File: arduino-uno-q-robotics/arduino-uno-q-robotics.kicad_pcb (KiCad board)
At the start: 4 copper layers, 68.6 x 53.3 mm, 11 parts, among them J1 Conn_02x30_Odd_Even, J2 Conn_02x30_Odd_Even, J3 Connector_FFC-FPC, J4 Connector_FFC-FPC, J5 Conn_02x13_Odd_Even, J6 Conn_02x04_Odd_Even, U1 LSM6DSO32

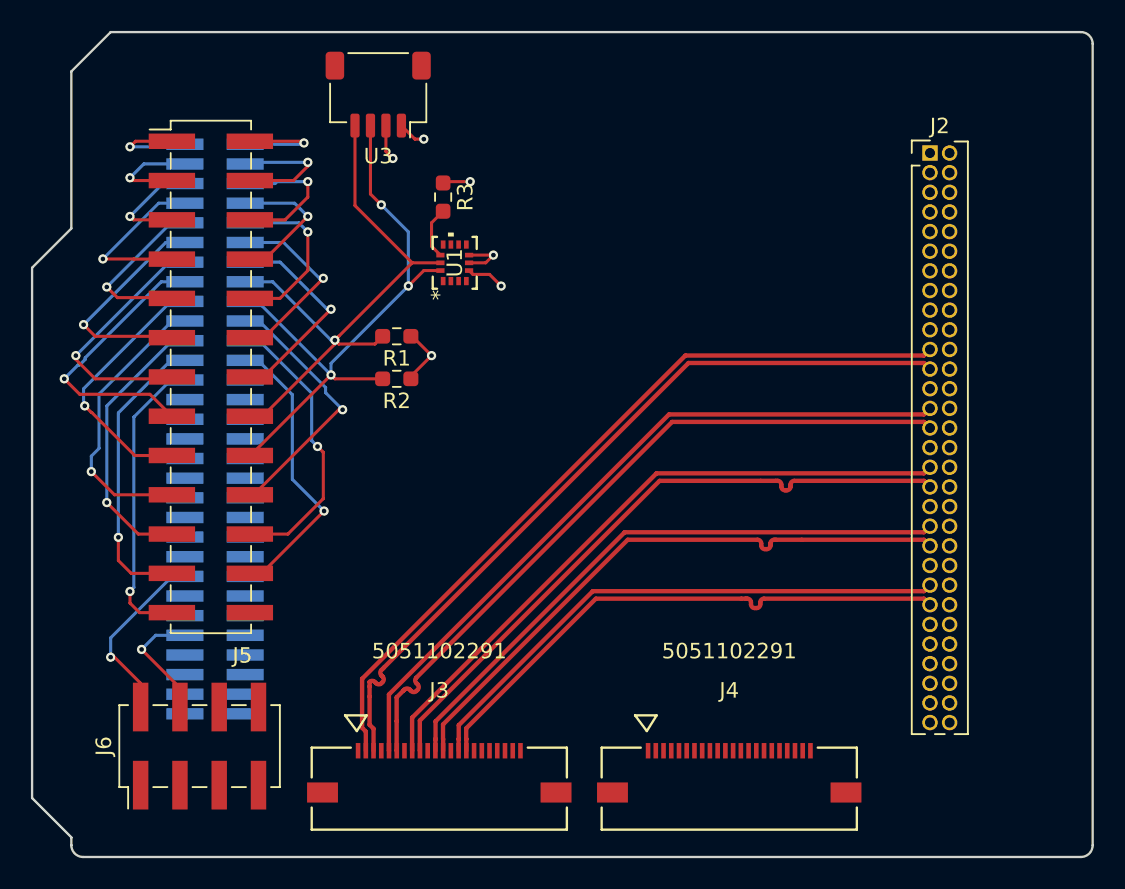
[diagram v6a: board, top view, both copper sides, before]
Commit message: Adjust JMISC/JMEDIA header spacing
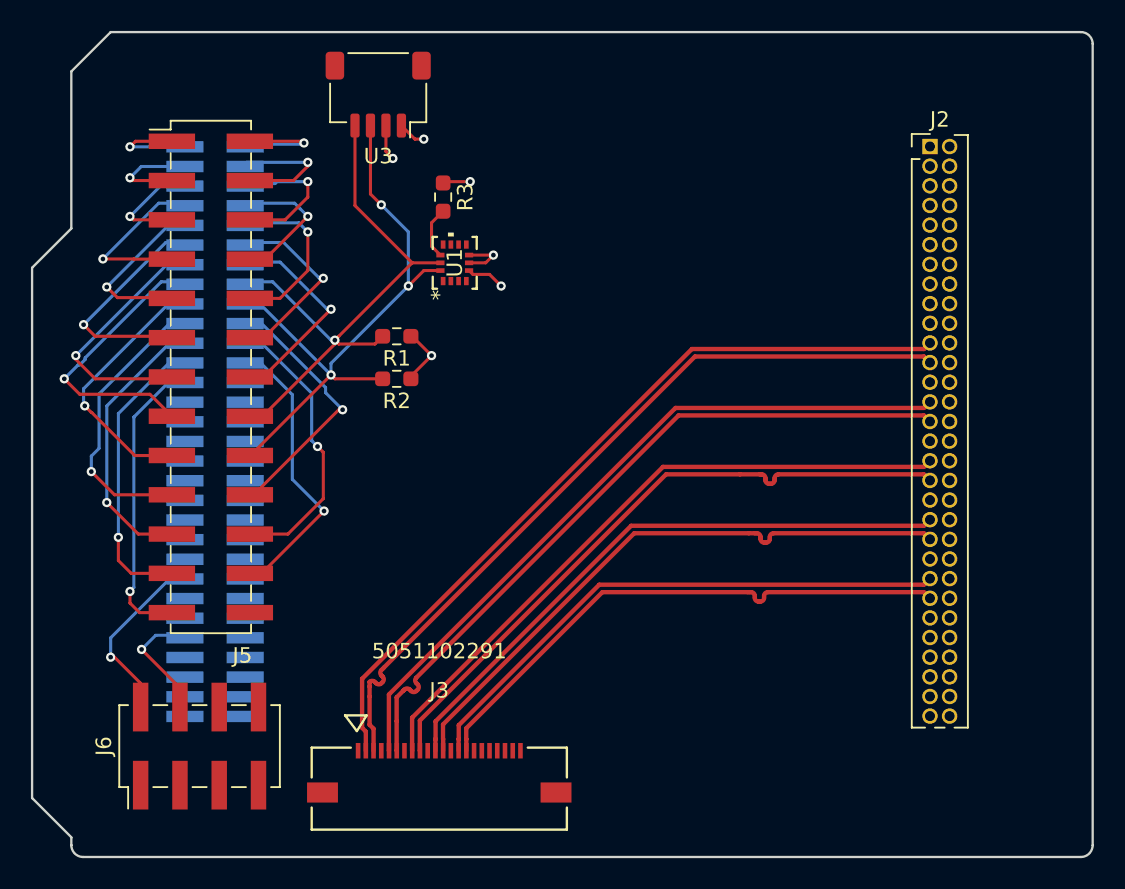
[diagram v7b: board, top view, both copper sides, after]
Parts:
- removed J4: Connector_FFC-FPC, robotics-footprints:CON_5051102291_MOL
- moved J2 0.42 mm to (172.5, 75.0)
- moved J1 0.17 mm to (126.2, 93.4)

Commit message: Add missing components to PCB editor
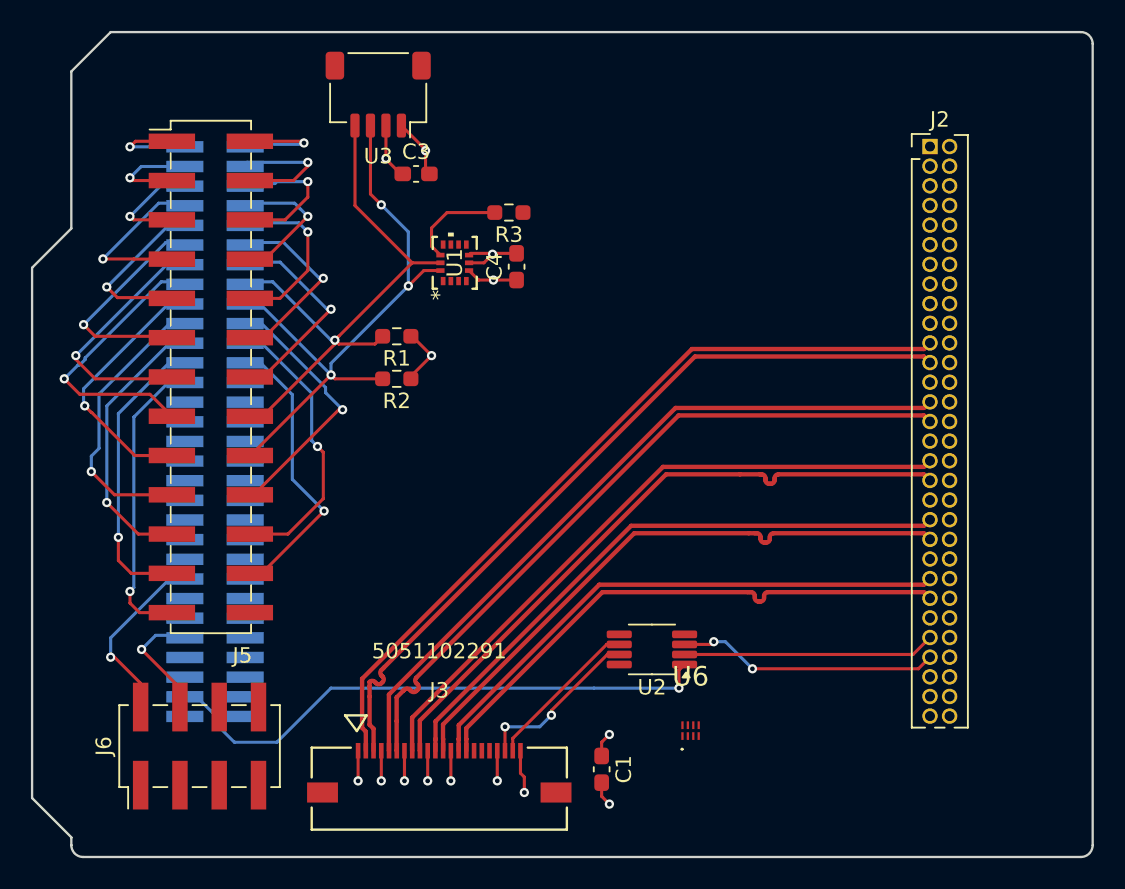
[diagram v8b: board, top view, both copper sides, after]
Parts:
- added C1: 0.1 uF, Capacitor_SMD:C_0603_1608Metric_Pad1.08x0.95mm_HandSolder, F.Cu at (151.2, 115.2)
- added C3: 0.1 uF, Capacitor_SMD:C_0603_1608Metric_Pad1.08x0.95mm_HandSolder, F.Cu at (139.2, 76.8)
- added C4: 0.1 uF, Capacitor_SMD:C_0603_1608Metric_Pad1.08x0.95mm_HandSolder, F.Cu at (145.8, 82.8)
- added U2: TCA9803, Package_SO:VSSOP-8_3x3mm_P0.65mm, F.Cu at (154.5, 107.5)
- added U6: ~, robotics-footprints:74LVC2T45GS115, F.Cu at (157.0, 112.8)
- moved R3 4.37 mm to (145.2, 79.2), turned to 180 degrees
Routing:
- net +1V8: track 0.00 -> 36.6 mm, vias 0 -> 1
- net /CCI_I2C_SDA0: track 0.00 -> 17.2 mm, vias 0 -> 2
- net GND: track 5.17 -> 22.1 mm, vias 2 -> 9
- net /CCI_I2C_SCL0: track 0.00 -> 16.3 mm
- net /SCL0_3.3V: track 0.00 -> 11.1 mm, vias 0 -> 2
- net /SDA0_3.3V: track 0.00 -> 10.2 mm
- net +3.3V: track 10.5 -> 15.3 mm, vias 4 -> 5
- net /CS: track 3.39 -> 6.49 mm
